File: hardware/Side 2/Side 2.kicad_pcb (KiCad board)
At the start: 2 copper layers, 126 x 214.2 mm, 4 parts

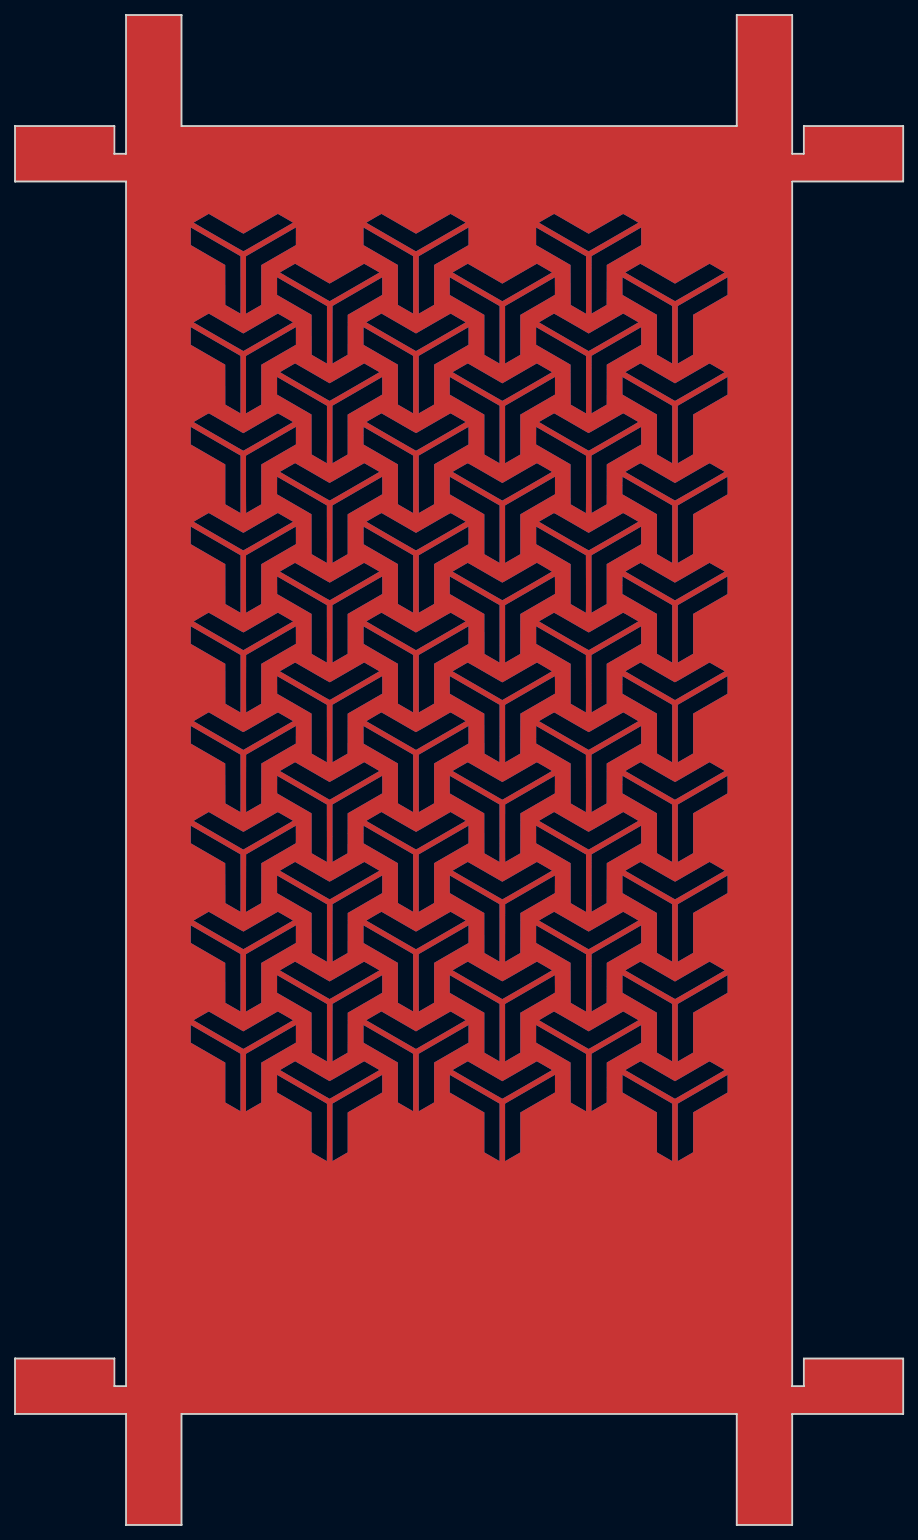
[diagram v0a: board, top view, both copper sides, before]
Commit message: Added reflective copper on inside Added version with cutout dinoskin Generated gerbers
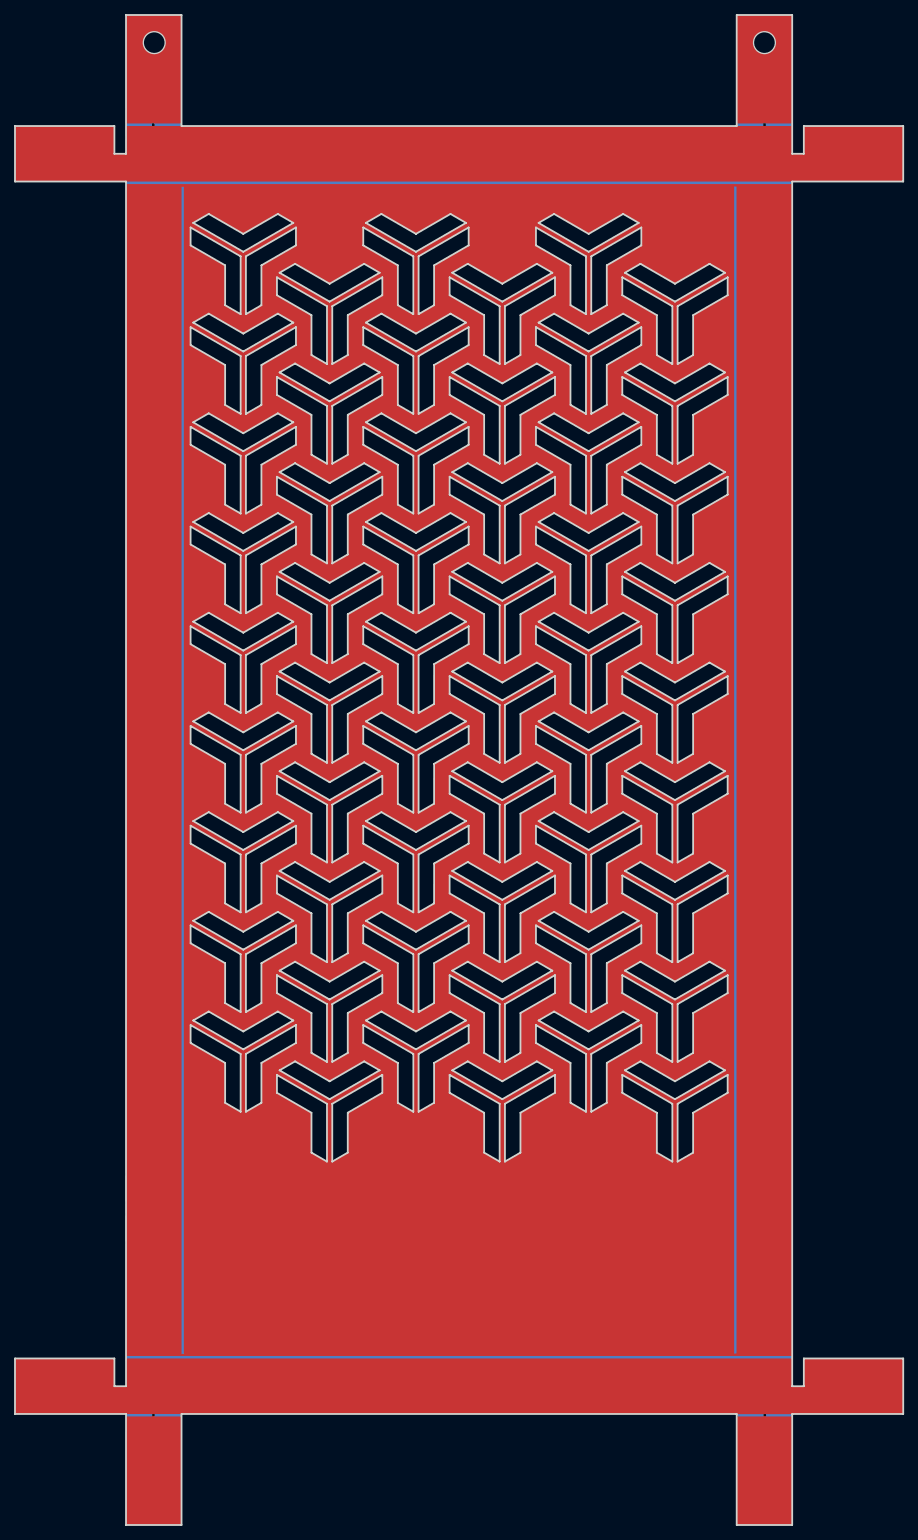
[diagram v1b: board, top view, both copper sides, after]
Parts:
- added REF**: Center_Hole_Dial_2.05, BamboulabFootprints:Center_Hole_Dial_2.05, F.Cu at (-27.9, 19.9)
- added REF**: Center_Hole_Dial_2.05, BamboulabFootprints:Center_Hole_Dial_2.05, F.Cu at (-122.8, 18.3)
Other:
- outline, holes or cut-outs redrawn

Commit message: God knows but a lot has changed
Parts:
- removed the G*** at (-79.8, 120.2)
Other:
- outline, holes or cut-outs redrawn
- board text added: "JLCJLCJLC"
